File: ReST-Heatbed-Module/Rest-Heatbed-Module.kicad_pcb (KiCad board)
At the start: 2 copper layers, 29.8 x 36.2 mm, 82 parts

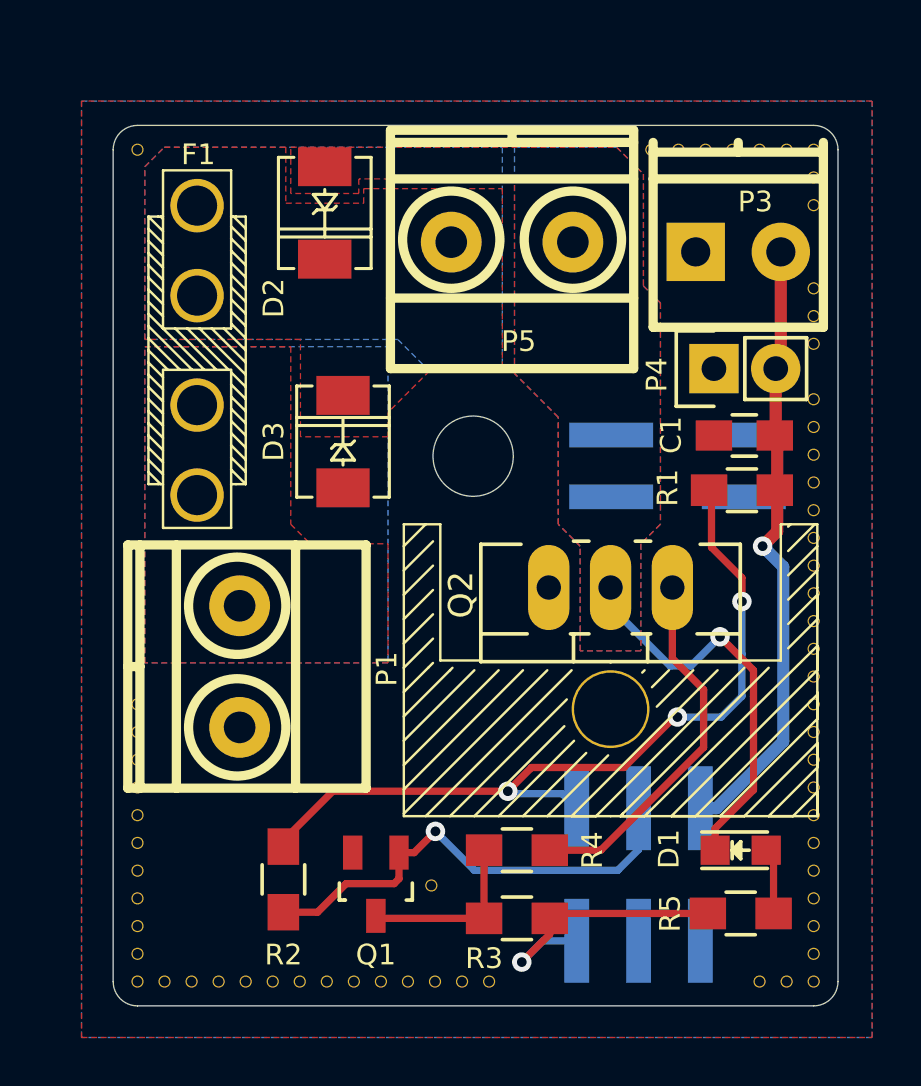
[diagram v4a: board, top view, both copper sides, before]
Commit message: Changes in Heatbed and Heater + F1 and F4 Pinout table with functions
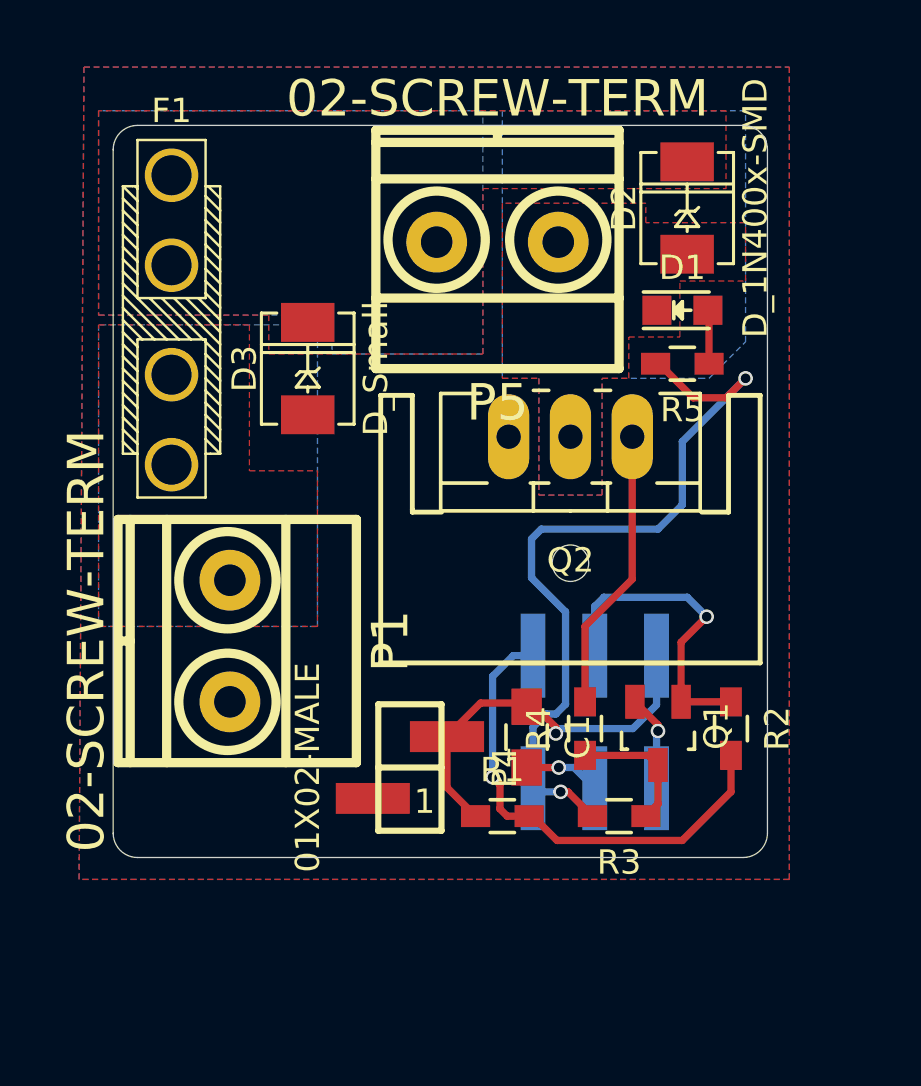
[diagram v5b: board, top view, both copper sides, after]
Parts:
- removed ? (x63): , ReST-Library:1pin
- removed ?: 1pin, ReST-Library:1pin
- removed P3: , ReST-Library:pt_1,5-2-3,5-h
- removed P6: , ReST-Library:bb02-hp04
- C1: value (none) -> 10uF
- D1: value (none) -> LED
- D2: value (none) -> D_1N400x-SMD
- D3: value (none) -> D_Small
- F1: value (none) -> 15A
- P1, P5: value (none) -> 02-SCREW-TERM
- P2: value (none) -> CONN_02X03
- P4: value (none) -> 01X02-MALE; footprint Pin_Headers:Pin_Header_Straight_1x02 -> ReST-Library:bb02-hy02a
- Q1: value (none) -> Q_BSH105/IRLML2502
- Q2: value (none) -> Q_AOT240L
- R1: value (none) -> 4.7K; footprint Resistors_SMD:R_0805_HandSoldering -> Resistors_SMD:R_0603_HandSoldering
- R2, R3: value (none) -> 100K; footprint Resistors_SMD:R_0805_HandSoldering -> Resistors_SMD:R_0603_HandSoldering
- R4: value (none) -> 22R; footprint Resistors_SMD:R_0805_HandSoldering -> Resistors_SMD:R_0603_HandSoldering
- R5: value (none) -> 150R; footprint Resistors_SMD:R_0805_HandSoldering -> Resistors_SMD:R_0603_HandSoldering
- moved R5 22.7 mm to (191.0, 67.4)
- moved D1 22.3 mm to (191.0, 65.2)
- moved P4 20.6 mm to (179.8, 84.0), turned to 270 degrees
- moved R2 19.4 mm to (193.0, 82.4), turned to 270 degrees
- moved R1 16.6 mm to (183.6, 86.0), turned to 0 degrees
- moved C1 15.3 mm to (184.6, 82.8), turned to 270 degrees
- moved D2 14.9 mm to (191.2, 61.0), turned to 90 degrees
- moved Q1 13.2 mm to (190.0, 82.6)
- moved P2 6.53 mm to (187.4, 82.1)
- moved Q2 6.42 mm to (186.4, 70.4)
- moved R3 5.94 mm to (188.4, 86.0), turned to 180 degrees
- moved R4 5.73 mm to (187.0, 82.4), turned to 90 degrees
- moved D3 3.33 mm to (175.6, 67.6)
- moved F1 1.63 mm to (170.0, 65.6)
- moved P1 1.12 mm to (172.4, 78.8)
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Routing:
- net +5V: track 11.5 -> 32.2 mm, vias 1 -> 2
- net /MOSFET: track 16.8 -> 0.00 mm, vias 1 -> 0
- net +3V3: track 33.8 -> 20.1 mm, vias 3 -> 1
- net /T0: track 25.4 -> 16.1 mm
- net GND: track 0.00 -> 7.12 mm, vias 0 -> 2
- net /PWM-HEATBED: track 19.3 -> 14.5 mm
- net Net-(Q2-Pad1): track 15.2 -> 11.7 mm
- net Net-(Q1-Pad3): track 7.29 -> 5.47 mm
- net Net-(D1-Pad2): track 2.72 -> 2.22 mm
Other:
- board size 29.8 x 36.2 mm -> 26.9 x 30.1 mm
- net class Default: via_dia 0.8 -> 0.6
- board text removed: "2 ounce board!!"
